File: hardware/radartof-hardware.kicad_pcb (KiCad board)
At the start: 6 copper layers, 25.4 x 66 mm, 110 parts, among them J1 Debug, J2 Camera, J3 1140084168, J4 FS USB, J5 J3026G01DNLT, U1 DF40HC(3.5)-80DS-0.4V(51), U10 TLV74315 SOT23-5, U11 LM3670MFX-3.3, U12 USBLC6-2SC6, U2 KC2016Z80.0000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

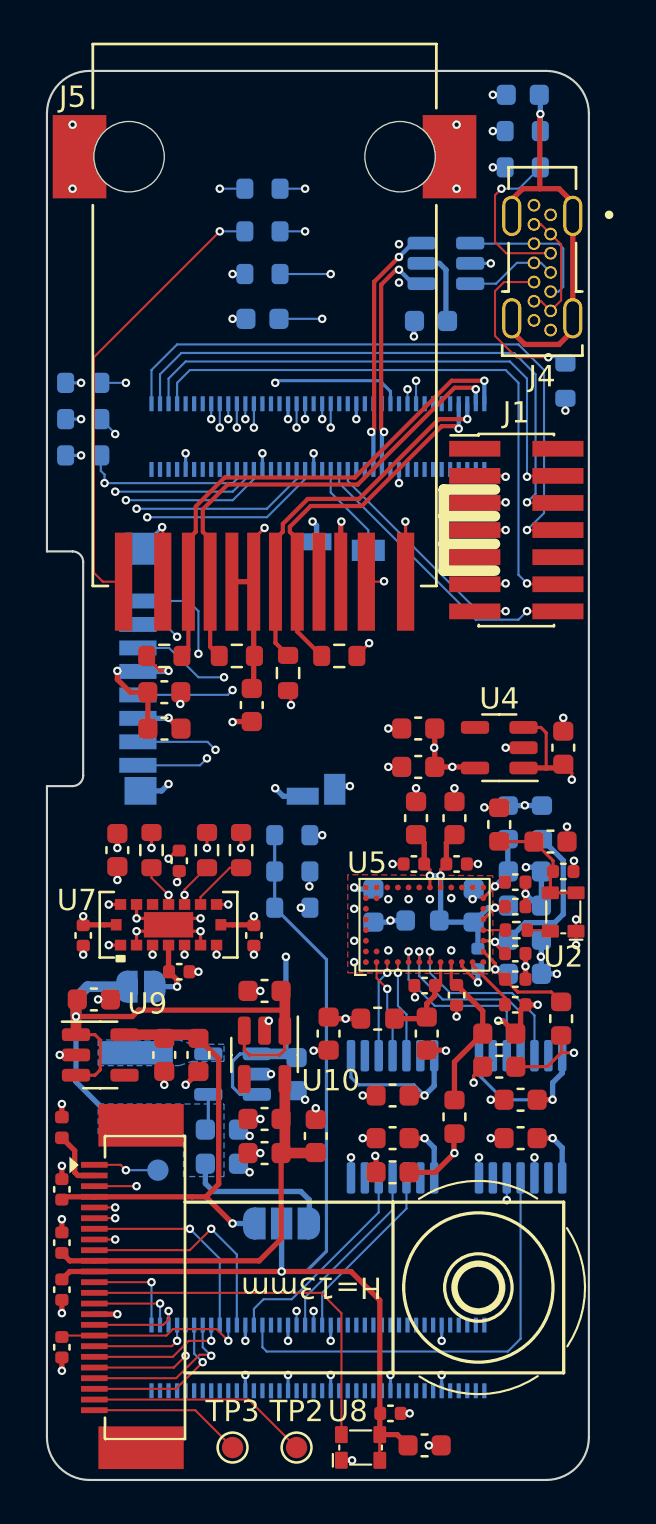
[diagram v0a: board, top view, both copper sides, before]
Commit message: Add testpoints, 0ohm, led, logos
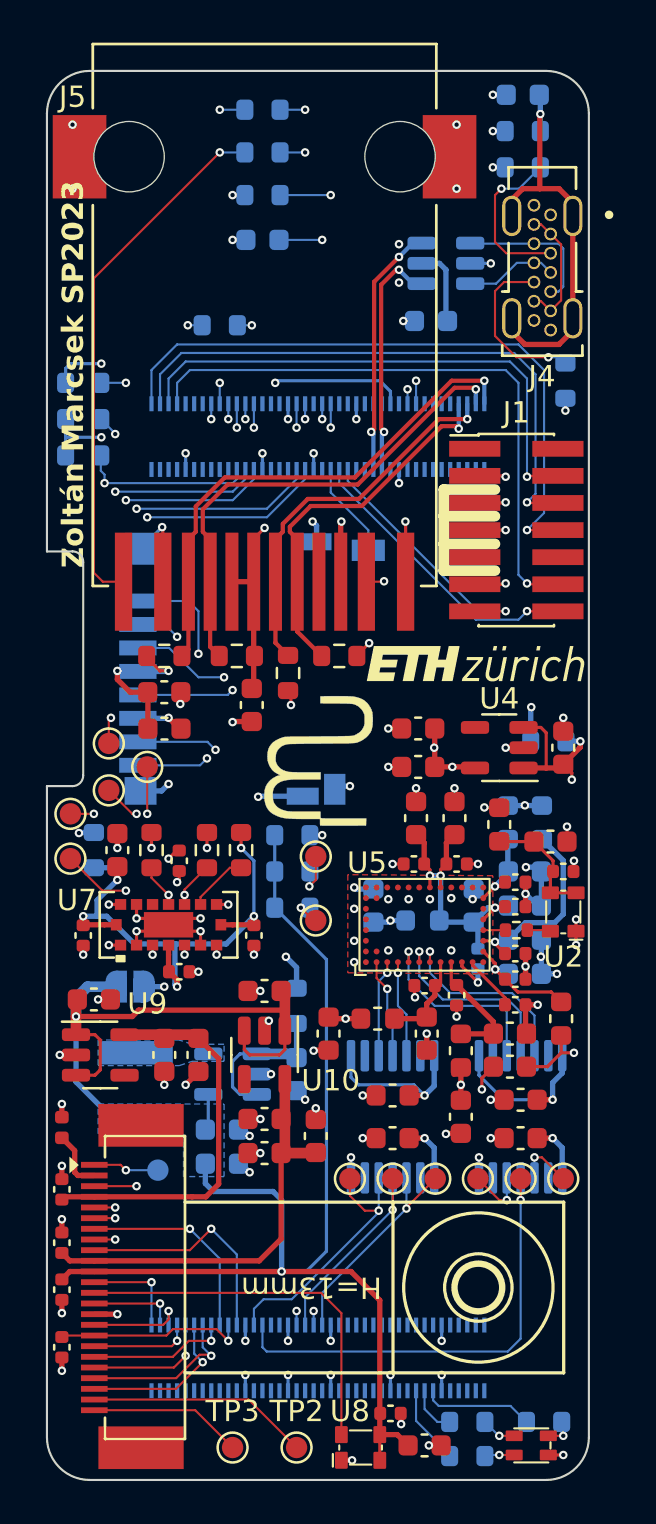
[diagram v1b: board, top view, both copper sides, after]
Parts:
- removed JP1: VIO Select, Jumper:SolderJumper-3_P1.3mm_Open_RoundedPad1.0x1.5mm
- added D1: Würth 150066M153000, 150066M153000:Würth_150066M153000, F.Cu at (160.0, 131.4)
- added R21: 0, Resistor_SMD:R_0603_1608Metric, B.Cu at (145.4, 78.9)
- added R22: 0, Resistor_SMD:R_0603_1608Metric, B.Cu at (149.0, 110.8)
- added R23: 0, Resistor_SMD:R_0603_1608Metric, B.Cu at (160.8, 98.4)
- added R24: 0, Resistor_SMD:R_0603_1608Metric, B.Cu at (139.5, 103.5)
- added R25: 1k, Resistor_SMD:R_0603_1608Metric, B.Cu at (157.0, 131.9)
- added R26: 470, Resistor_SMD:R_0603_1608Metric, B.Cu at (157.0, 130.3)
- added R27: 220, Resistor_SMD:R_0603_1608Metric, B.Cu at (160.6, 130.3)
- added TP10: TOF_LPn, TestPoint:TestPoint_Pad_D1.0mm, F.Cu at (138.4, 101.8)
- added TP11: SCL3, TestPoint:TestPoint_Pad_D1.0mm, F.Cu at (140.2, 100.7)
- added TP12: SDA3, TestPoint:TestPoint_Pad_D1.0mm, F.Cu at (142.0, 99.6)
- added TP13: TOF_INT, TestPoint:TestPoint_Pad_D1.0mm, F.Cu at (138.4, 103.9)
- added TP14: TOF_RST, TestPoint:TestPoint_Pad_D1.0mm, F.Cu at (140.2, 98.5)
- added TP15: SDA1, TestPoint:TestPoint_Pad_D1.0mm, F.Cu at (149.9, 103.8)
- added TP16: SCL1, TestPoint:TestPoint_Pad_D1.0mm, F.Cu at (149.9, 106.8)
- added TP4: MOSI, TestPoint:TestPoint_Pad_D1.0mm, F.Cu at (155.5, 118.9)
- added TP5: SCK, TestPoint:TestPoint_Pad_D1.0mm, F.Cu at (153.5, 118.9)
- added TP6: RADAR_INT, TestPoint:TestPoint_Pad_D1.0mm, F.Cu at (151.5, 118.9)
- added TP7: NSS, TestPoint:TestPoint_Pad_D1.0mm, F.Cu at (161.5, 118.9)
- added TP8: RADAR_nRST, TestPoint:TestPoint_Pad_D1.0mm, F.Cu at (159.5, 118.9)
- added TP9: MISO, TestPoint:TestPoint_Pad_D1.0mm, F.Cu at (157.5, 118.9)
- moved C11 4.12 mm to (156.7, 116.0), turned to -90 degrees
- moved R18 3.70 mm to (147.4, 70.8)
- moved R19 3.70 mm to (147.4, 68.8)
- moved R9 3.70 mm to (147.4, 72.8)
- moved C34 3.70 mm to (147.4, 74.9)
- moved L4 3.11 mm to (156.7, 112.9)
- moved C1 0.50 mm to (159.0, 113.7)
- moved C12 0.50 mm to (159.0, 112.1)
- moved JP2 0.50 mm to (141.2, 109.9)
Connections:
- C1 pad 1: +3.3V -> Vradar
- C26 pad 1: +3.3V -> Vradar
- C28 pad 1: +3.3V -> VTOF
- C29 pad 1: +3.3V -> VTOF
- C30 pad 1: +3.3V -> VTOF
- C31 pad 1: +3.3V -> VTOF
- C32 pad 1: VD -> VCAM
- C33 pad 1: VD -> VCAM
- C36 pad 1: +3.3VP -> VCAM
- C41 pad 1: VD -> VCAM
- C42 pad 1: +3.3VP -> VCAM
- C46 pad 1: +5V -> /Camera/5v_tof
- C47 pad 1: +3.3VP -> VCAM
- C48 pad 1: +3.3VP -> VCAM
- C57 pad 1: +3.3V -> Vradar
- C59 pad 1: +3.3V -> Vradar
- J2 pad 11: VD -> VCAM
- J3 pad 1: /Portenta/SDC_D2 -> Net-(J3-DAT2)
- JP2 pad 1: +3.3VP -> VCAM
- L1 pad 1: +3.3V -> Vradar
- L8 pad 2: +3.3VP -> VCAM
- R10 pad 1: VD -> VCAM
- R11 pad 1: VD -> VCAM
- R6 pad 1: +3.3V -> VTOF
- R8 pad 1: VD -> VCAM
- U1 pad J2_63: unconnected-(U1B-PWM_3-PadJ2_63) -> /Portenta/nLEDR
- U1 pad J2_65: unconnected-(U1B-PWM_4-PadJ2_65) -> /Portenta/nLEDG
- U1 pad J2_67: unconnected-(U1B-PWM_5-PadJ2_67) -> /Portenta/nLEDB
- U10 pad 1: +3.3VP -> VCAM
- U10 pad 3: +3.3VP -> VCAM
- U11 pad 1: +5V -> /Camera/5v_tof
- U11 pad 3: +5V -> /Camera/5v_tof
- U11 pad 4: +3.3VP -> VCAM
- U3 pad 1: +3.3V -> Vradar
- U4 pad 1: +3.3V -> Vradar
- U4 pad 3: +3.3V -> Vradar
- U6 pad 1: +3.3V -> Vradar
- U7 pad A4: +3.3V -> VTOF
- U7 pad B1: +3.3V -> VTOF
- U7 pad B7: +3.3V -> VTOF
- U8 pad 1: VD -> VCAM
- U8 pad 4: VD -> VCAM
- U9 pad 1: +3.3VP -> VCAM
- U9 pad 3: +3.3VP -> VCAM
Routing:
- net VCAM: track 0.00 -> 88.4 mm, vias 0 -> 2
- net VD: track 49.9 -> 0.00 mm, vias 1 -> 0
- net Vradar: track 0.00 -> 42.9 mm, vias 0 -> 5
- net +3.3VP: track 40.3 -> 0.00 mm, vias 1 -> 0
- net VTOF: track 0.00 -> 25.7 mm, vias 0 -> 5
- net Net-(J3-DAT2): track 0.00 -> 22.1 mm, vias 0 -> 2
- net +3.3V: track 56.5 -> 38.8 mm, vias 26 -> 20
- net /Portenta/SDC_D2: track 17.2 -> 4.98 mm
- net +5V: track 43.6 -> 35.0 mm
- net /Camera/5v_tof: track 0.00 -> 7.30 mm
- net /Portenta/nLEDB: track 0.00 -> 5.24 mm
- net Net-(J5-Pad11): track 25.0 -> 28.8 mm
- net /Portenta/nLEDR: track 0.00 -> 3.71 mm
- net /Connectors/ETH_LED2: track 11.9 -> 15.6 mm
- net Net-(J5-Pad1): track 21.2 -> 24.9 mm
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- added copper zone on B.Cu, net VCAM
- removed copper zone on B.Cu, net +3.3VP
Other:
- board text added: "Zoltán Marcsek SP2023"

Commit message: Final fixes, manufacturing
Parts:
- L1, L2, L3, L4, L5, L6, L7: value L -> BLM15PX471SZ1D; footprint Inductor_SMD:L_0603_1608Metric -> Inductor_SMD:L_0402_1005Metric
- L8: value ASPI-4030S-100M-T -> 74438336022; footprint Inductor_SMD:L_Abracon_ASPI-4030S -> Inductor_SMD:L_Wuerth_MAPI-3020
- L9: renamed from FB1; value FerriteBead -> BLM15PX471SZ1D
- U11: value LM3670MFX-3.3 -> LM3671MF-3.3
- moved L1 1.41 mm to (161.2, 110.0), turned to 180 degrees
- moved C4 1.00 mm to (151.5, 112.1)
- moved L8 0.54 mm to (141.7, 114.0)
- moved L2 0.51 mm to (153.3, 111.3)
- moved C1 0.50 mm to (159.5, 113.7)
- moved L3 0.42 mm to (158.8, 102.6)
- moved C12 0.40 mm to (158.6, 112.1)
- moved L5 0.40 mm to (160.5, 102.6)
- moved L7 0.40 mm to (158.9, 102.6)
- moved C11 0.20 mm to (156.5, 116.0)
- moved L4 0.20 mm to (156.5, 112.9)
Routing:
- net VCAM: track 88.4 -> 93.7 mm
- net Vradar: track 42.9 -> 41.3 mm
- net /Radar/VDD_RF: track 14.3 -> 15.7 mm
- net GND: track 89.9 -> 91.0 mm, vias 113 -> 112
- net /Radar/VDD_LF: track 5.49 -> 4.68 mm
- net /Camera/5v_tof: track 7.30 -> 6.51 mm

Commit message: Manufacturing
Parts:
- moved L5 3.09 mm to (161.8, 105.4)
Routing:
- net unconnected-(J4-VBUS-PadA4): track 5.94 -> 0.00 mm
- net /Radar/VDD_PLL: track 8.88 -> 5.79 mm
- net +1V8: track 26.2 -> 27.3 mm, vias 9 -> 10
- net /Portenta/RADAR_INT: track 12.5 -> 11.8 mm
- net /Portenta/SPI2_SCK: track 10.1 -> 9.40 mm
- net GND: track 91.0 -> 90.8 mm, vias 112 -> 129
- added copper zone on B.Cu, net GND
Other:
- board text added: "Zoltán Marcsek"
